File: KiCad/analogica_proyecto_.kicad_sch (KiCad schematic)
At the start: 30 parts, among them U8 INA219AxD, U9 INA219AxD

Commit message: Sensor Hall y LED mas o menos definitivos
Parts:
- TP_3V3, TP_GND1, TP_GND2, TP_GND3, TP_GNDPWM1, TP_GNDPWM2, TP_GNDPWM3, TP_GNDPWM4: footprint (none) -> TestPoint:TestPoint_Pad_D1.5mm
- TP_5V0: renamed from TP_5V; footprint (none) -> TestPoint:TestPoint_Pad_D1.5mm
- TP_PWM_M1, TP_PWM_M2, TP_Rshunt1, TP_Rshunt2: footprint (none) -> TestPoint:TestPoint_2Pads_Pitch2.54mm_Drill0.8mm
- TP_SCL0: renamed from TP_SCL; footprint (none) -> TestPoint:TestPoint_2Pads_Pitch2.54mm_Drill0.8mm
- TP_SDA0: renamed from TP_SDA; footprint (none) -> TestPoint:TestPoint_2Pads_Pitch2.54mm_Drill0.8mm
- TP_Vbat0: renamed from TP_Vbat; footprint (none) -> TestPoint:TestPoint_Pad_D1.5mm
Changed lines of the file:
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@@
 		(dnp no)
 		(fields_autoplaced yes)
-		(property "Reference" "TP_SDA"
+		(property "Reference" "TP_SDA0"
 			(at 69.85 63.5 0)
 			(effects
@@
 			)
 		)
-		(property "Footprint" ""
+		(property "Footprint" "TestPoint:TestPoint_2Pads_Pitch2.54mm_Drill0.8mm"
 			(at 69.85 68.58 0)
 			(effects
@@
 			(project "projecte_sostre"
 				(path "/12dc51a9-2603-4518-b497-f55f3848c2a7/e4e158bc-7b20-484f-8f94-ff020121094e"
-					(reference "TP_SDA")
+					(reference "TP_SDA0")
 					(unit 1)
 				)
@@
 			)
 		)
-		(property "Footprint" ""
+		(property "Footprint" "TestPoint:TestPoint_Pad_D1.5mm"
 			(at 57.15 139.7 0)
 			(effects
@@
 		(dnp no)
 		(fields_autoplaced yes)
-		(property "Reference" "TP_5V"
+		(property "Reference" "TP_5V0"
 			(at 35.56 135.1279 0)
 			(effects
@@
 			)
 		)
-		(property "Footprint" ""
+		(property "Footprint" "TestPoint:TestPoint_Pad_D1.5mm"
 			(at 38.1 139.7 0)
 			(effects
@@
 			(project "projecte_sostre"
 				(path "/12dc51a9-2603-4518-b497-f55f3848c2a7/e4e158bc-7b20-484f-8f94-ff020121094e"
-					(reference "TP_5V")
+					(reference "TP_5V0")
 					(unit 1)
 				)
@@
 			)
 		)
-		(property "Footprint" ""
+		(property "Footprint" "TestPoint:TestPoint_2Pads_Pitch2.54mm_Drill0.8mm"
 			(at 69.85 114.3 0)
 			(effects
@@
 			)
 		)
-		(property "Footprint" ""
+		(property "Footprint" "TestPoint:TestPoint_2Pads_Pitch2.54mm_Drill0.8mm"
 			(at 69.85 105.41 0)
 			(effects
@@
 			)
 		)
-		(property "Footprint" ""
+		(property "Footprint" "TestPoint:TestPoint_Pad_D1.5mm"
 			(at 80.01 148.59 0)
 			(effects
@@
 			)
 		)
-		(property "Footprint" ""
+		(property "Footprint" "TestPoint:TestPoint_2Pads_Pitch2.54mm_Drill0.8mm"
 			(at 69.85 96.52 0)
 			(effects
@@
 		(dnp no)
 		(fields_autoplaced yes)
-		(property "Reference" "TP_SCL"
+		(property "Reference" "TP_SCL0"
 			(at 69.85 72.39 0)
 			(effects
@@
 			)
 		)
-		(property "Footprint" ""
+		(property "Footprint" "TestPoint:TestPoint_2Pads_Pitch2.54mm_Drill0.8mm"
 			(at 69.85 77.47 0)
 			(effects
@@
 			(project "projecte_sostre"
 				(path "/12dc51a9-2603-4518-b497-f55f3848c2a7/e4e158bc-7b20-484f-8f94-ff020121094e"
-					(reference "TP_SCL")
+					(reference "TP_SCL0")
 					(unit 1)
 				)
@@
 			)
 		)
-		(property "Footprint" ""
+		(property "Footprint" "TestPoint:TestPoint_Pad_D1.5mm"
 			(at 57.15 148.59 0)
 			(effects
@@
 			)
 		)
-		(property "Footprint" ""
+		(property "Footprint" "TestPoint:TestPoint_Pad_D1.5mm"
 			(at 80.01 129.54 0)
 			(effects
@@
 			)
 		)
-		(property "Footprint" ""
+		(property "Footprint" "TestPoint:TestPoint_2Pads_Pitch2.54mm_Drill0.8mm"
 			(at 69.85 87.63 0)
 			(effects
@@
 			)
 		)
-		(property "Footprint" ""
+		(property "Footprint" "TestPoint:TestPoint_Pad_D1.5mm"
 			(at 80.01 139.7 0)
 			(effects
@@
 			)
 		)
-		(property "Footprint" ""
+		(property "Footprint" "TestPoint:TestPoint_Pad_D1.5mm"
 			(at 80.01 157.48 0)
 			(effects
@@
 			)
 		)
-		(property "Footprint" ""
+		(property "Footprint" "TestPoint:TestPoint_Pad_D1.5mm"
 			(at 57.15 130.81 0)
 			(effects
@@
 		(dnp no)
 		(fields_autoplaced yes)
-		(property "Reference" "TP_Vbat"
+		(property "Reference" "TP_Vbat0"
 			(at 35.56 144.0179 0)
 			(effects
@@
 			)
 		)
-		(property "Footprint" ""
+		(property "Footprint" "TestPoint:TestPoint_Pad_D1.5mm"
 			(at 38.1 148.59 0)
 			(effects
@@
 			(project "projecte_sostre"
 				(path "/12dc51a9-2603-4518-b497-f55f3848c2a7/e4e158bc-7b20-484f-8f94-ff020121094e"
-					(reference "TP_Vbat")
+					(reference "TP_Vbat0")
 					(unit 1)
 				)
@@
 			)
 		)
-		(property "Footprint" ""
+		(property "Footprint" "TestPoint:TestPoint_Pad_D1.5mm"
 			(at 38.1 130.81 0)
 			(effects

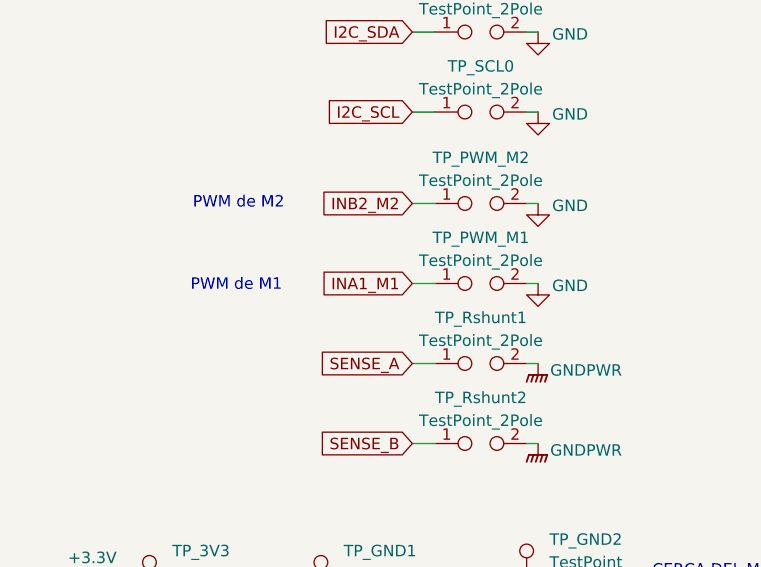
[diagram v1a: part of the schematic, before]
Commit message: Layout con pocos cables en capa Bot pero todavai hay que hacer cambios que nos dijo el Miercoles pasado
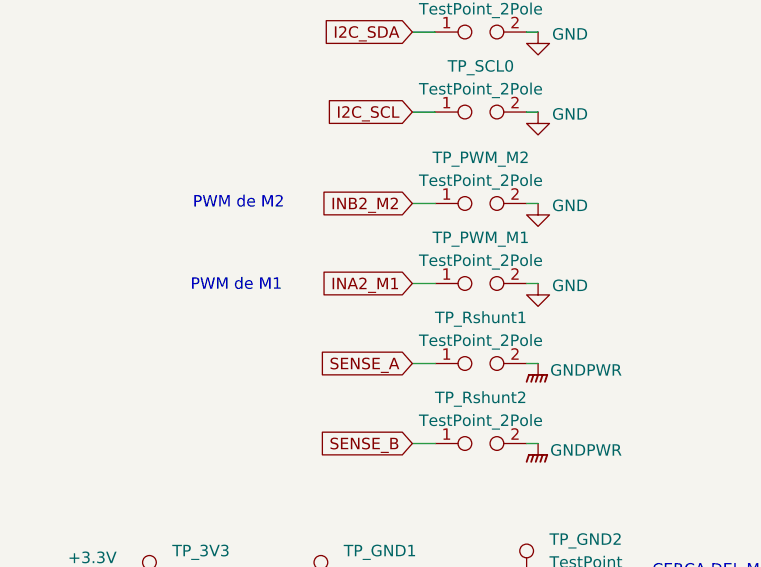
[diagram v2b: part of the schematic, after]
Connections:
- net INA1_M1 renamed INA2_M1
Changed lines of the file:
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@@
 		)
 	)
-	(global_label "INA1_M1"
+	(global_label "INA2_M1"
 		(shape input)
 		(at 62.23 96.52 180)

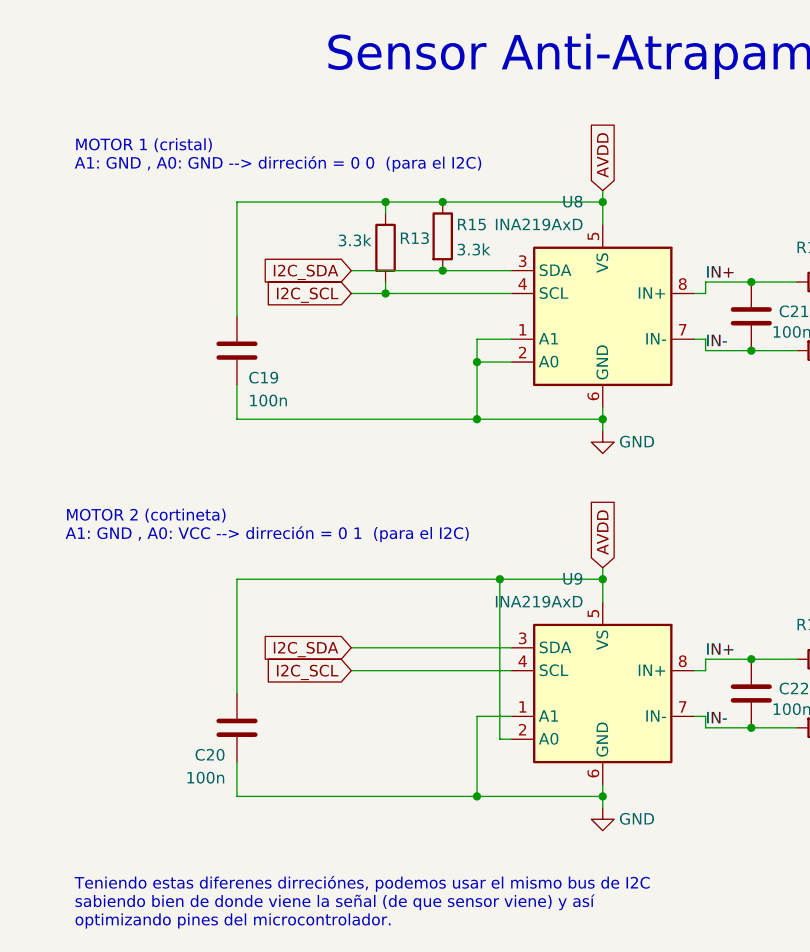
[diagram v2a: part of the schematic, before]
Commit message: Cambios Layout propuestos para mejorar posicionamiento
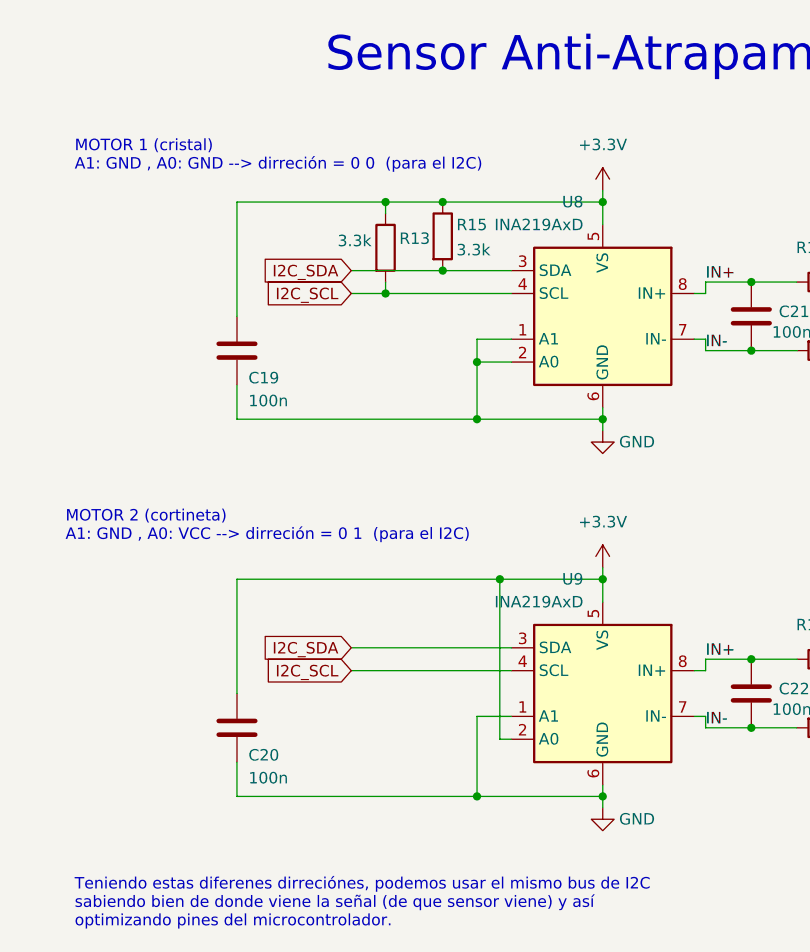
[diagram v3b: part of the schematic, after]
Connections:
- net AVDD is gone; now on net +3.3V: C19.1, C20.1, R13.1, R15.1, U8.5 (VS), U9.2 (A0), U9.5 (VS)
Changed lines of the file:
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@@
-		)
-	)
-	(global_label "AVDD"
-		(shape input)
-		(at 193.04 60.96 90)
-		(fields_autoplaced yes)
-		(effects
-			(font
-				(size 1.27 1.27)
-			)
-			(justify left)
-		)
-		(property "Intersheetrefs" "${INTERSHEET_REFS}"
-			(at 193.04 53.2576 90)
-			(effects
-				(font
-					(size 1.27 1.27)
-				)
-				(justify left)
-				(hide yes)
-			)
 		)
 	)
@@
 		)
 	)
-	(global_label "AVDD"
-		(shape input)
-		(at 193.04 102.87 90)
-		(fields_autoplaced yes)
-		(effects
-			(font
-				(size 1.27 1.27)
-			)
-			(justify left)
-		)
-		(property "Intersheetrefs" "${INTERSHEET_REFS}"
-			(at 193.04 95.1676 90)
-			(effects
-				(font
-					(size 1.27 1.27)
-				)
-				(justify left)
-				(hide yes)
-			)
-		)
-	)
 	(symbol
 		(lib_id "Sensor_Energy:INA219AxD")
@@
 	)
 	(symbol
+		(lib_id "power:+3.3V")
+		(at 193.04 60.96 0)
+		(unit 1)
+		(exclude_from_sim no)
+		(in_bom yes)
+		(on_board yes)
+		(dnp no)
+		(fields_autoplaced yes)
+		(property "Reference" "#PWR099"
+			(at 193.04 64.77 0)
+			(effects
+				(font
+					(size 1.27 1.27)
+				)
+				(hide yes)
+			)
+		)
+		(property "Value" "+3.3V"
+			(at 193.04 55.88 0)
+			(effects
+				(font
+					(size 1.27 1.27)
+				)
+			)
+		)
+		(property "Footprint" ""
+			(at 193.04 60.96 0)
+			(effects
+				(font
+					(size 1.27 1.27)
+				)
+				(hide yes)
+			)
+		)
+		(property "Datasheet" ""
+			(at 193.04 60.96 0)
+			(effects
+				(font
+					(size 1.27 1.27)
+				)
+				(hide yes)
+			)
+		)
+		(property "Description" "Power symbol creates a global label with name \"+3.3V\""
+			(at 193.04 60.96 0)
+			(effects
+				(font
+					(size 1.27 1.27)
+				)
+				(hide yes)
+			)
+		)
+		(pin "1"
+		)
+		(instances
+			(project "projecte_sostre"
+				(path "/12dc51a9-2603-4518-b497-f55f3848c2a7/e4e158bc-7b20-484f-8f94-ff020121094e"
+					(reference "#PWR099")
+					(unit 1)
+				)
+			)
+		)
+	)
+	(symbol
 		(lib_id "Connector:TestPoint_2Pole")
 		(at 69.85 114.3 0)
@@
 		(lib_id "Device:C")
 		(at 152.4 120.65 0)
-		(mirror y)
 		(unit 1)
 		(exclude_from_sim no)
@@
 		(dnp no)
 		(property "Reference" "C20"
-			(at 151.13 123.698 0)
+			(at 153.67 123.698 0)
 			(effects
 				(font
@@
 		)
 		(property "Value" "100n"
-			(at 151.13 126.238 0)
+			(at 153.67 126.238 0)
 			(effects
 				(font
@@
 		)
 		(property "Footprint" "Capacitor_SMD:C_0805_2012Metric"
-			(at 151.4348 124.46 0)
+			(at 153.3652 124.46 0)
 			(effects
 				(font
@@
 					(unit 1)
 				)
+			)
+		)
+	)
+	(symbol
+		(lib_id "power:+3.3V")
+		(at 193.04 102.87 0)
+		(unit 1)
+		(exclude_from_sim no)
+		(in_bom yes)
+		(on_board yes)
+		(dnp no)
+		(fields_autoplaced yes)
+		(property "Reference" "#PWR098"
+			(at 193.04 106.68 0)
+			(effects
+				(font
+					(size 1.27 1.27)
+				)
+				(hide yes)
+			)
+		)
+		(property "Value" "+3.3V"
+			(at 193.04 97.79 0)
+			(effects
+				(font
+					(size 1.27 1.27)
+				)
+			)
+		)
+		(property "Footprint" ""
+			(at 193.04 102.87 0)
+			(effects
+				(font
+					(size 1.27 1.27)
+				)
+				(hide yes)
+			)
+		)
+		(property "Datasheet" ""
+			(at 193.04 102.87 0)
+			(effects
+				(font
+					(size 1.27 1.27)
+				)
+				(hide yes)
+			)
+		)
+		(property "Description" "Power symbol creates a global label with name \"+3.3V\""
+			(at 193.04 102.87 0)
+			(effects
+				(font
+					(size 1.27 1.27)
+				)
+				(hide yes)
+			)
+		)
+		(pin "1"
+		)
+		(instances
+			(project "projecte_sostre"
+				(path "/12dc51a9-2603-4518-b497-f55f3848c2a7/e4e158bc-7b20-484f-8f94-ff020121094e"
+					(reference "#PWR098")
+					(unit 1)
+				)

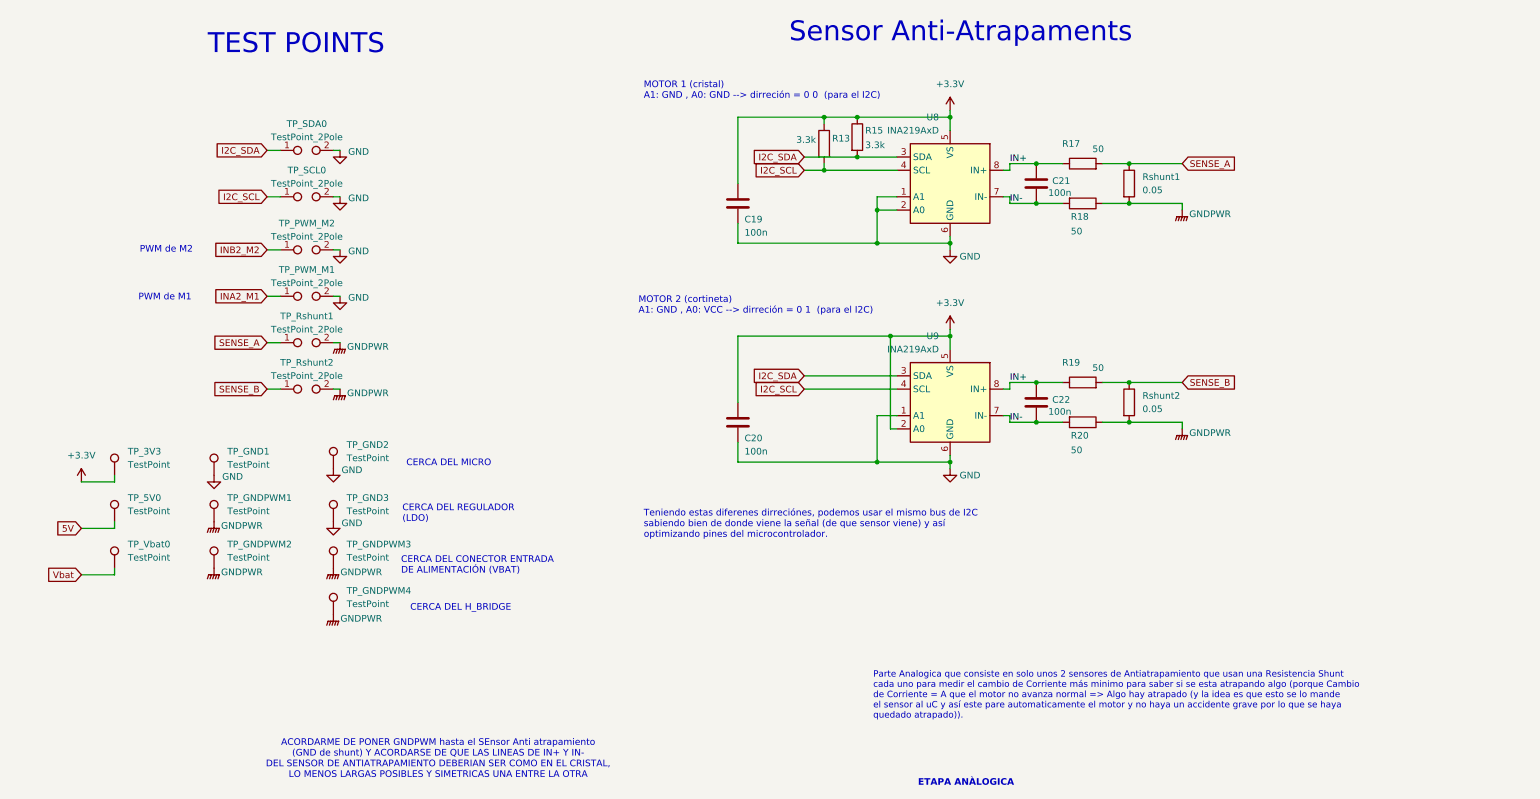
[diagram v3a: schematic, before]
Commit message: PCB casi acabada, despues de revisión de ayer 27/04 y cambio en componente CAN, que se vera reflejado en README y en DB
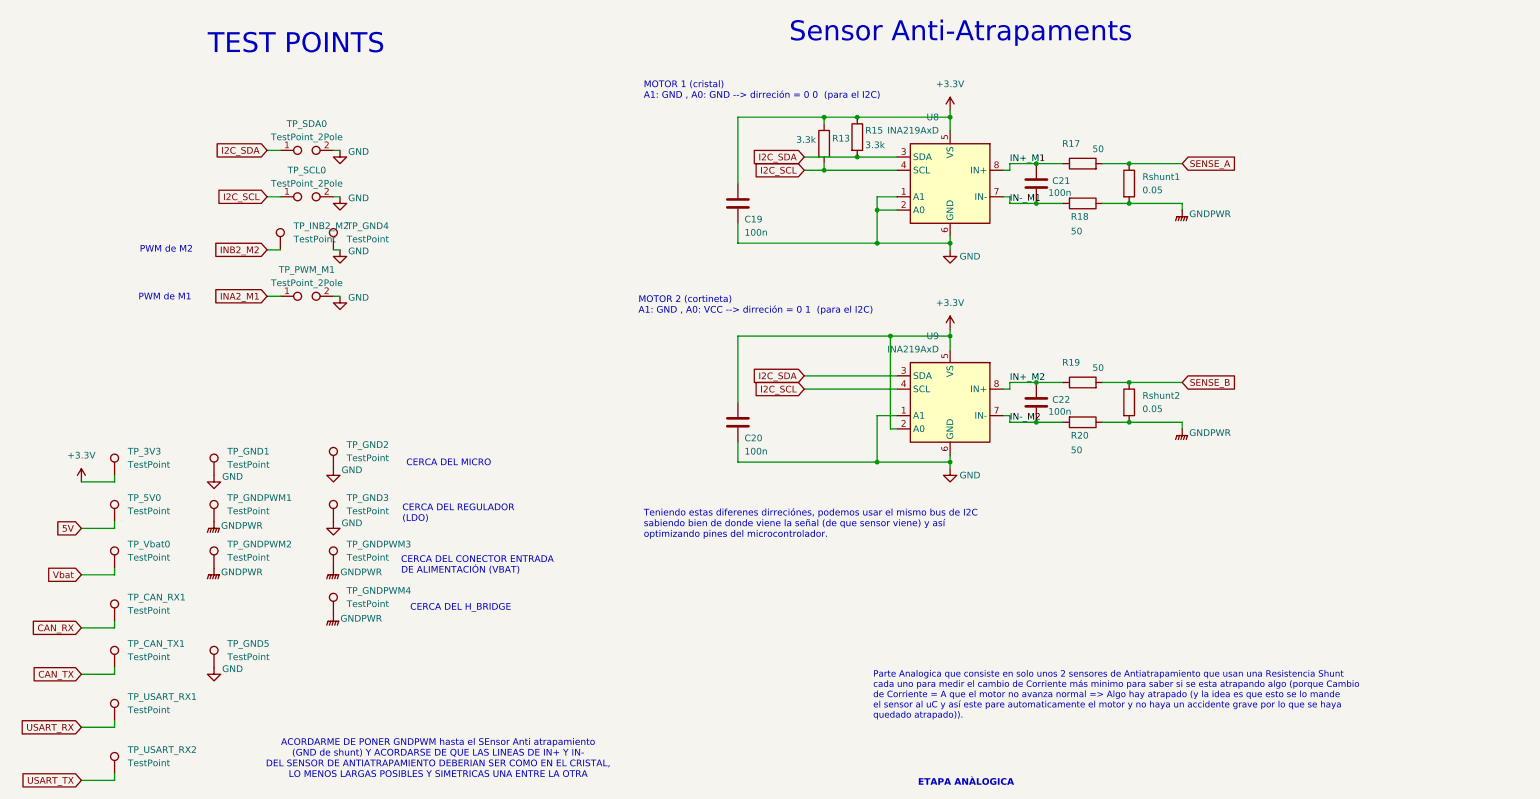
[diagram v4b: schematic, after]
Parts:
- removed TP_PWM_M2, TP_Rshunt1, TP_Rshunt2: TestPoint_2Pole, TestPoint:TestPoint_2Pads_Pitch2.54mm_Drill0.8mm, symbol Connector:TestPoint_2Pole
- added TP_CAN_RX1, TP_CAN_TX1, TP_GND4, TP_GND5, TP_INB2_M2, TP_USART_RX1, TP_USART_RX2: TestPoint, TestPoint:TestPoint_Keystone_5000-5004_Miniature, symbol Connector:TestPoint
- TP_3V3, TP_5V0, TP_GND1, TP_GND2, TP_GND3, TP_GNDPWM1, TP_GNDPWM2, TP_GNDPWM3, TP_GNDPWM4, TP_Vbat0: footprint TestPoint:TestPoint_Pad_D1.5mm -> TestPoint:TestPoint_Keystone_5000-5004_Miniature
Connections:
- net GND: now also TP_GND4.1, TP_GND5.1
- net INB2_M2: now also TP_INB2_M2.1
- net IN+ renamed IN+_M1
- net IN+_M1: no longer C22.1, R19.1, U9.8 (IN+)
- net IN- renamed IN-_M1
- net IN-_M1: no longer C22.2, R20.2, U9.7 (IN-)
- new net CAN_RX: TP_CAN_RX1.1
- new net CAN_TX: TP_CAN_TX1.1
- new net IN+_M2: C22.1, R19.1, U9.8 (IN+)
- new net IN-_M2: C22.2, R20.2, U9.7 (IN-)
- new net USART_RX: TP_USART_RX1.1
- new net USART_TX: TP_USART_RX2.1

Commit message: Layout definitivo
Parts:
- removed TP_PWM_M1, TP_SCL0, TP_SDA0: TestPoint_2Pole, TestPoint:TestPoint_2Pads_Pitch2.54mm_Drill0.8mm, symbol Connector:TestPoint_2Pole
- added GND10, PWM_M1, SCL0, SDA0: TestPoint, TestPoint:TestPoint_Keystone_5000-5004_Miniature, symbol Connector:TestPoint
- renumbered TP_GND1 to GND1, TP_GNDPWM1 to GND2, TP_GNDPWM2 to GND3, TP_GND5 to GND4, TP_GND2 to GND5, TP_GND3 to GND6, TP_GNDPWM3 to GND7, TP_GNDPWM4 to GND8, TP_GND4 to GND9, TP_INB2_M2 to PWM_M2, TP_CAN_RX1 to RX1, TP_USART_RX1 to RX2, Rshunt1 to Rsht1, Rshunt2 to Rsht2, TP_CAN_TX1 to TX1, TP_USART_RX2 to TX2
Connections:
- net GND: now also GND2.1, GND3.1, GND7.1, GND8.1, GND10.1
- net GNDPWR: no longer GND2.1, GND3.1, GND7.1, GND8.1
- net I2C_SCL: now also SCL0.1
- net I2C_SDA: now also SDA0.1
- net INA2_M1: now also PWM_M1.1
